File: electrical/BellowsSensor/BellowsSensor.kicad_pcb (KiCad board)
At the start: 2 copper layers, 26 x 18 mm, 5 parts, among them U1 ABPMRRV001PD2A3

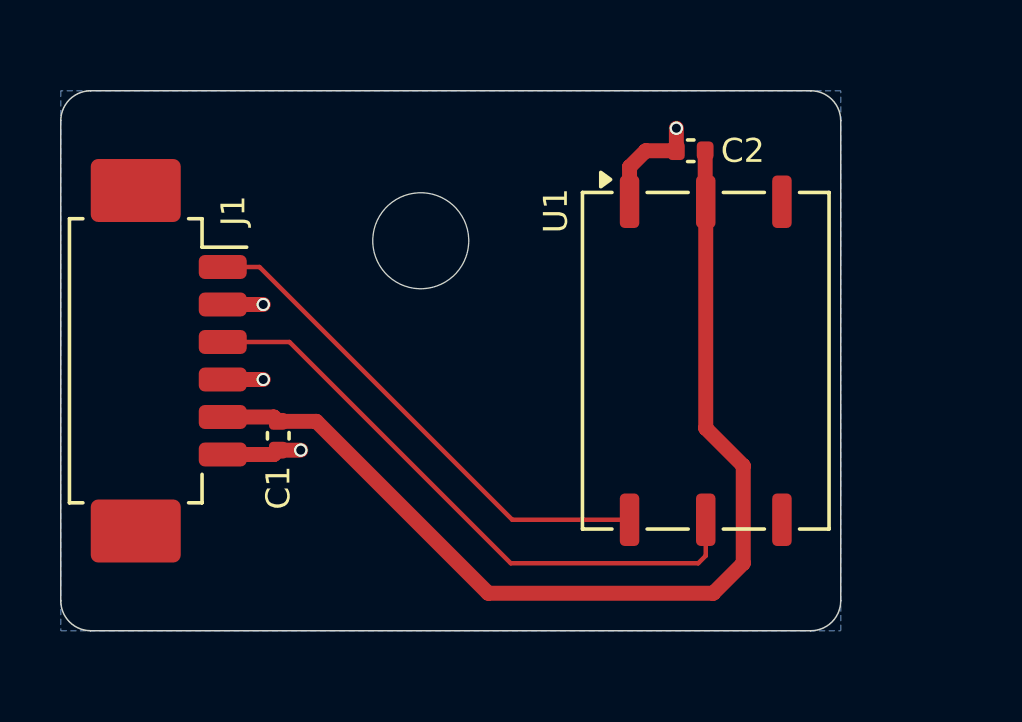
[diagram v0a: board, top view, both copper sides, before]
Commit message: Replace pressure sensor part
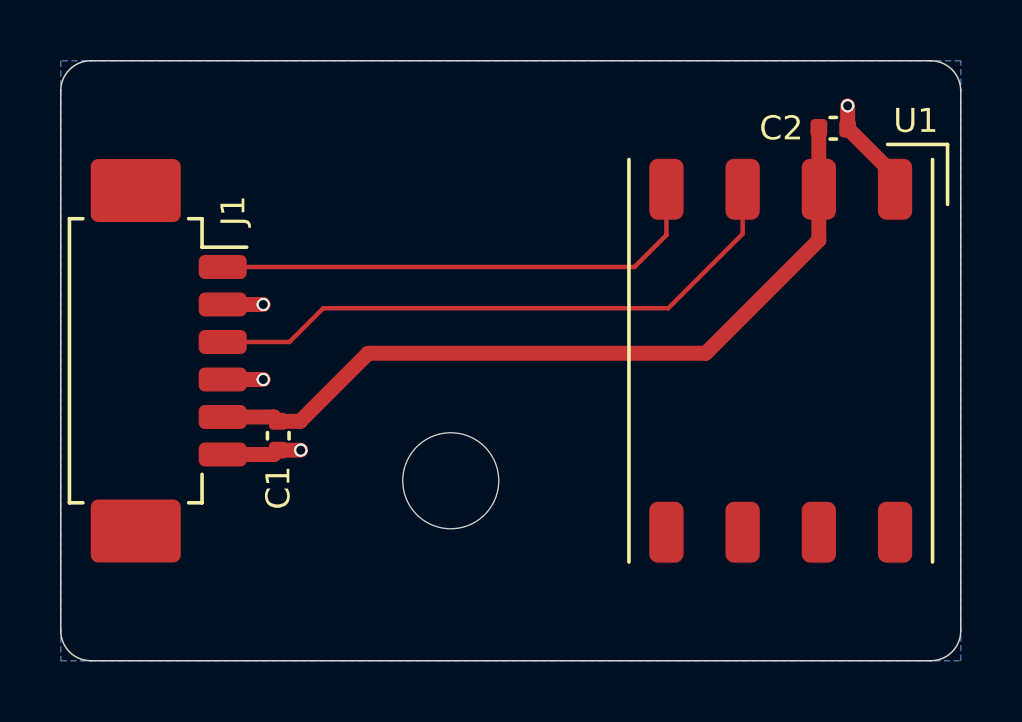
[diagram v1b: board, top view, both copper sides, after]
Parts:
- U1: value ABPMRRV001PD2A3 -> HSCMRRV001PD2A3; footprint MidiConcertina:Honeywell_ABPMRRx -> MidiConcertina:Honeywell_HSCMRRx
- moved H1 8.06 mm to (141.0, 108.0)
- moved C2 4.81 mm to (153.8, 96.2), turned to 0 degrees
- moved U1 2.50 mm to (152.0, 104.0), turned to -90 degrees
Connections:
- U1 pad 3: unconnected-(U1-INT-Pad3) -> /I2C_SDA
- U1 pad 4: unconnected-(U1-NC-Pad4) -> /I2C_SCL
- U1 pad 5: /I2C_SDA -> unconnected-(U1-NC-Pad5)
- U1 pad 6: /I2C_SCL -> unconnected-(U1-NC-Pad6)
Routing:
- net +3.3V: track 34.5 -> 26.2 mm
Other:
- board size 26 x 18 mm -> 30 x 20 mm

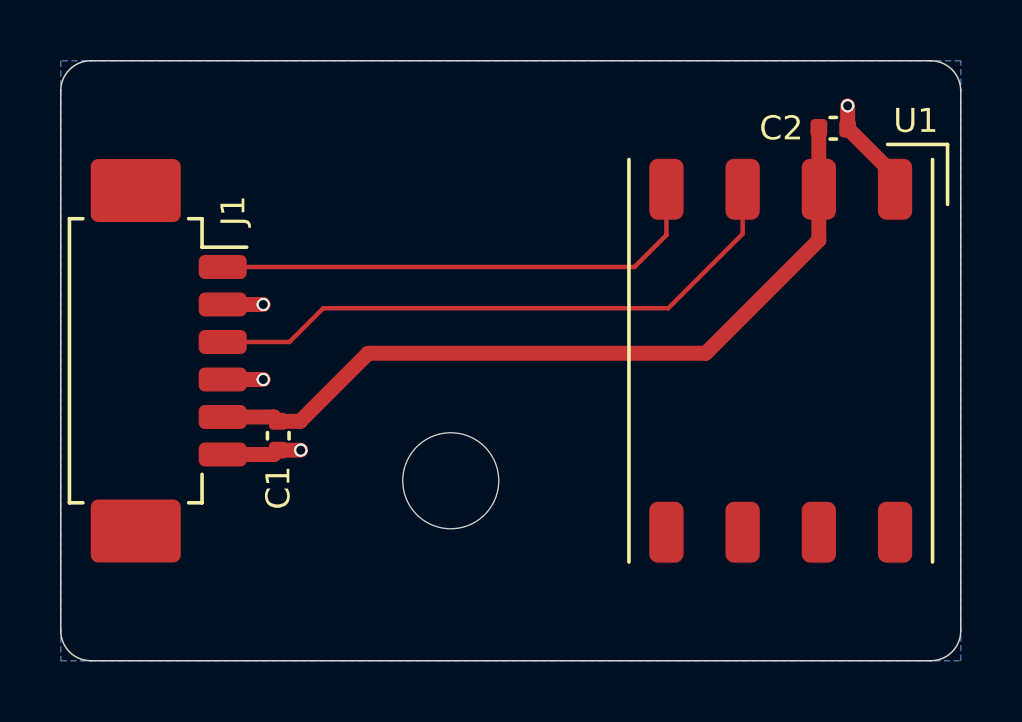
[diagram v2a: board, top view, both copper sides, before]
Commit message: Switch pressure sensors again
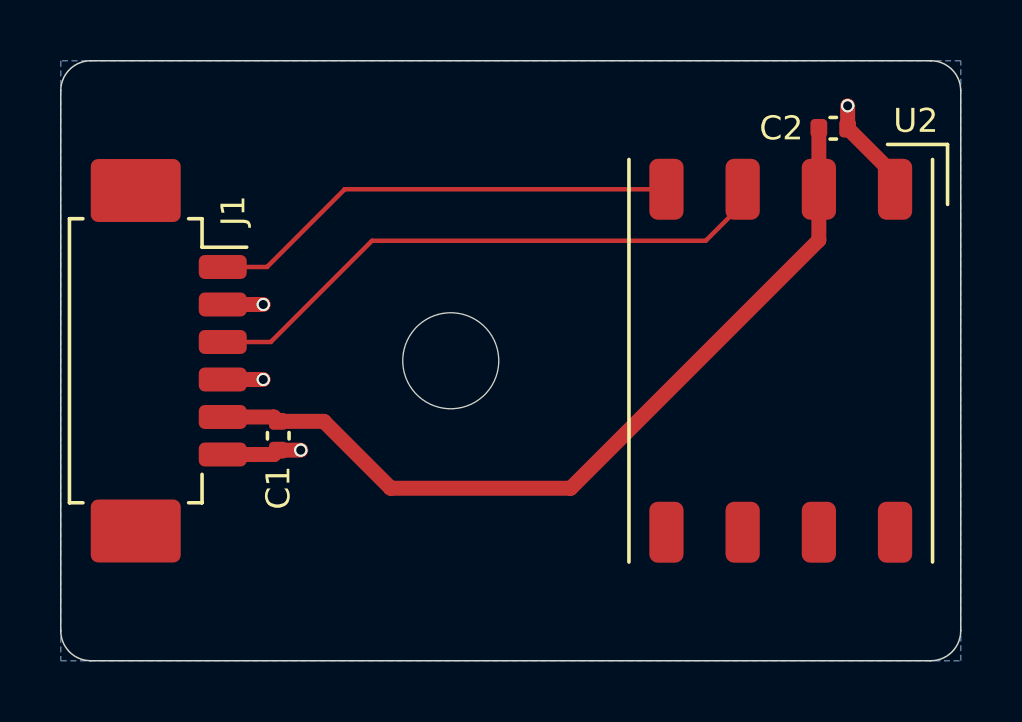
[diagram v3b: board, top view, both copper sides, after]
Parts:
- removed U1: HSCMRRV001PD2A3, MidiConcertina:Honeywell_HSCMRRx
- added U2: ELVH-001D-HRRJ-C-N2A4, MidiConcertina:Amphenol_ELVH-x-xJ-x-x, F.Cu at (152.0, 104.0)
- moved H1 4.00 mm to (141.0, 104.0)
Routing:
- net +3.3V: track 26.2 -> 28.0 mm
- net /I2C_SCL: track 16.8 -> 15.9 mm
- net /I2C_SDA: track 20.3 -> 19.7 mm

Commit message: Use REVISION var to fill silkscreen
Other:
- board text added: "MIDI Concertina Bellows Sensor - Rev ${REVISION}"
- board text removed: "MIDI Concertina Bellows Sensor - Rev 1"
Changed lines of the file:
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@@
 	(title_block
 		(title "MIDI Concertina Bellows Sensor")
+		(rev "1")
 		(comment 1 "https://ohwr.org/cern_ohl_s_v2.pdf")
 		(comment 2 "Licensed under CERN-OHL-S v2 or any later version")
@@
 		(layer "Edge.Cuts")
 	)
-	(gr_text "MIDI Concertina\nBellows Sensor - Rev 1"
+	(gr_text "MIDI Concertina\nBellows Sensor - Rev ${REVISION}"
 		(at 156 96 0)
 		(layer "B.SilkS")

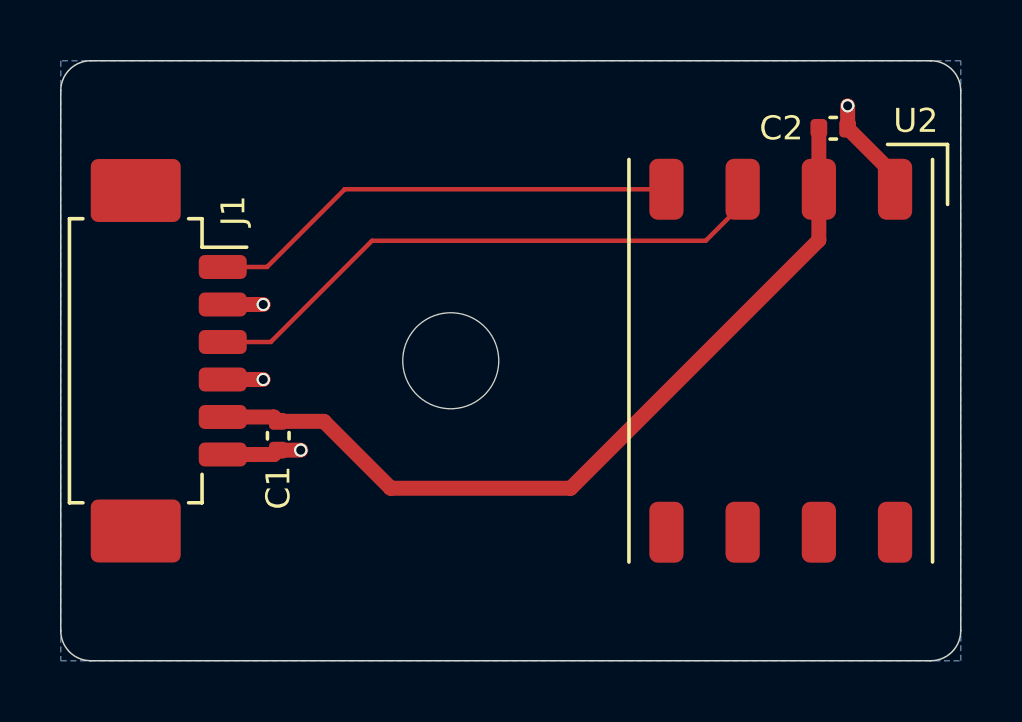
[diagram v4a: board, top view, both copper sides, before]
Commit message: Replace PicoBlade connectors with SKEDD
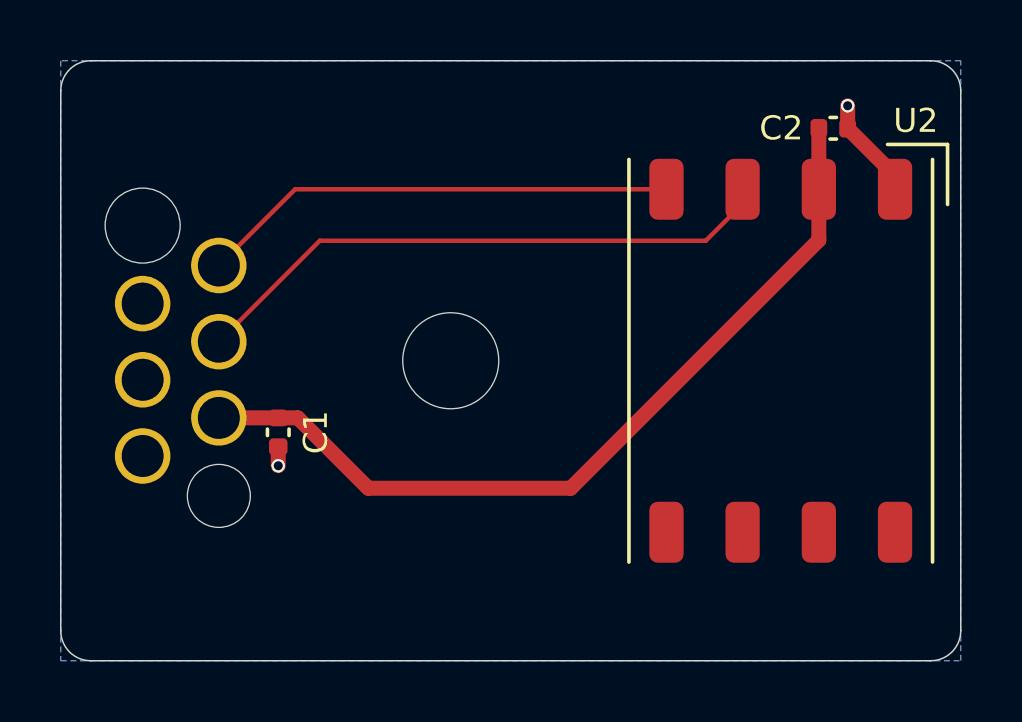
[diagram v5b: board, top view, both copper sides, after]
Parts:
- J1: value ~ -> I2C; footprint Connector_Molex:Molex_PicoBlade_53261-0671_1x06-1MP_P1.25mm_Horizontal -> MidiConcertina:Wuerth_WR-WST_490107670612_2x03_P2.54mm_SKEDD; moved to B.Cu
- moved J1 1.00 mm to (132.0, 104.0), turned to 180 degrees
- moved C1 0.11 mm to (135.2, 106.4)
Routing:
- net GND: track 8.80 -> 4.07 mm, vias 4 -> 2
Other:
- board text added: "MIDI Concertina Bellows Sensor Rev ${REVISION}"
- board text removed: "MIDI Concertina Bellows Sensor - Rev ${REVISION}"

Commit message: Relabel components
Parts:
- renumbered U2 to U1
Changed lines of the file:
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@@
 	(net 3 "/I2C_SCL")
 	(net 4 "/I2C_SDA")
-	(net 5 "unconnected-(U2-NC-Pad5)")
-	(net 6 "unconnected-(U2-NC-Pad7)")
-	(net 7 "unconnected-(U2-NC-Pad8)")
-	(net 8 "unconnected-(U2-NC-Pad6)")
+	(net 5 "unconnected-(U1-NC-Pad5)")
+	(net 6 "unconnected-(U1-NC-Pad7)")
+	(net 7 "unconnected-(U1-NC-Pad8)")
+	(net 8 "unconnected-(U1-NC-Pad6)")
 	(footprint "Capacitor_SMD:C_0402_1005Metric"
 		(layer "F.Cu")
@@
 		(at 152 104 -90)
 		(tags "sop sensor pressure")
-		(property "Reference" "U2"
+		(property "Reference" "U1"
 			(at -8 -4.5 0)
 			(layer "F.SilkS")
@@
 			(layers "F.Cu" "F.Mask" "F.Paste")
 			(roundrect_rratio 0.25)
-			(net 5 "unconnected-(U2-NC-Pad5)")
+			(net 5 "unconnected-(U1-NC-Pad5)")
 			(pinfunction "NC")
 			(pintype "no_connect")
@@
 			(layers "F.Cu" "F.Mask" "F.Paste")
 			(roundrect_rratio 0.25)
-			(net 8 "unconnected-(U2-NC-Pad6)")
+			(net 8 "unconnected-(U1-NC-Pad6)")
 			(pinfunction "NC")
 			(pintype "no_connect")
@@
 			(layers "F.Cu" "F.Mask" "F.Paste")
 			(roundrect_rratio 0.25)
-			(net 6 "unconnected-(U2-NC-Pad7)")
+			(net 6 "unconnected-(U1-NC-Pad7)")
 			(pinfunction "NC")
 			(pintype "no_connect")
@@
 			(layers "F.Cu" "F.Mask" "F.Paste")
 			(roundrect_rratio 0.25)
-			(net 7 "unconnected-(U2-NC-Pad8)")
+			(net 7 "unconnected-(U1-NC-Pad8)")
 			(pinfunction "NC")
 			(pintype "no_connect")
